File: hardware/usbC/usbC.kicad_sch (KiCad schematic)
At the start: 17 parts, among them J2 Conn_01x02, J3 Conn_01x02, J4 Conn_01x01, J5 Conn_01x02, J6 Conn_01x01, J7 Conn_01x01, J8 Conn_01x01, J9 Connector, USB-TYPE-C-16P, U1 USBLC6-2SC6, U2 AMS1117-3.3

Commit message: wip
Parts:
- removed J4, J6, J7, J8: Conn_01x01, Connector_PinHeader_1.00mm:PinHeader_1x01_P1.00mm_Vertical, symbol Connector_Generic:Conn_01x01
- added J1: Conn_01x02, LIB_S2B-ZR_LF__SN_:S2BZRLFSN, symbol Connector_Generic:Conn_01x02
- added J6, J7: Conn_01x02, Connector_PinHeader_2.54mm:PinHeader_1x02_P2.54mm_Vertical, symbol Connector_Generic:Conn_01x02
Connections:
- net D+: now also J6.1 (Pin_1)
- net D-: now also J6.2 (Pin_2)
- net GND: now also J1.2 (Pin_2), J7.1 (Pin_1)
- net VCC: now also J1.1 (Pin_1)
- net at F1.1, J9.A9B4 (VBUS), J9.B9A4 (VBUS): now also J7.2 (Pin_2)

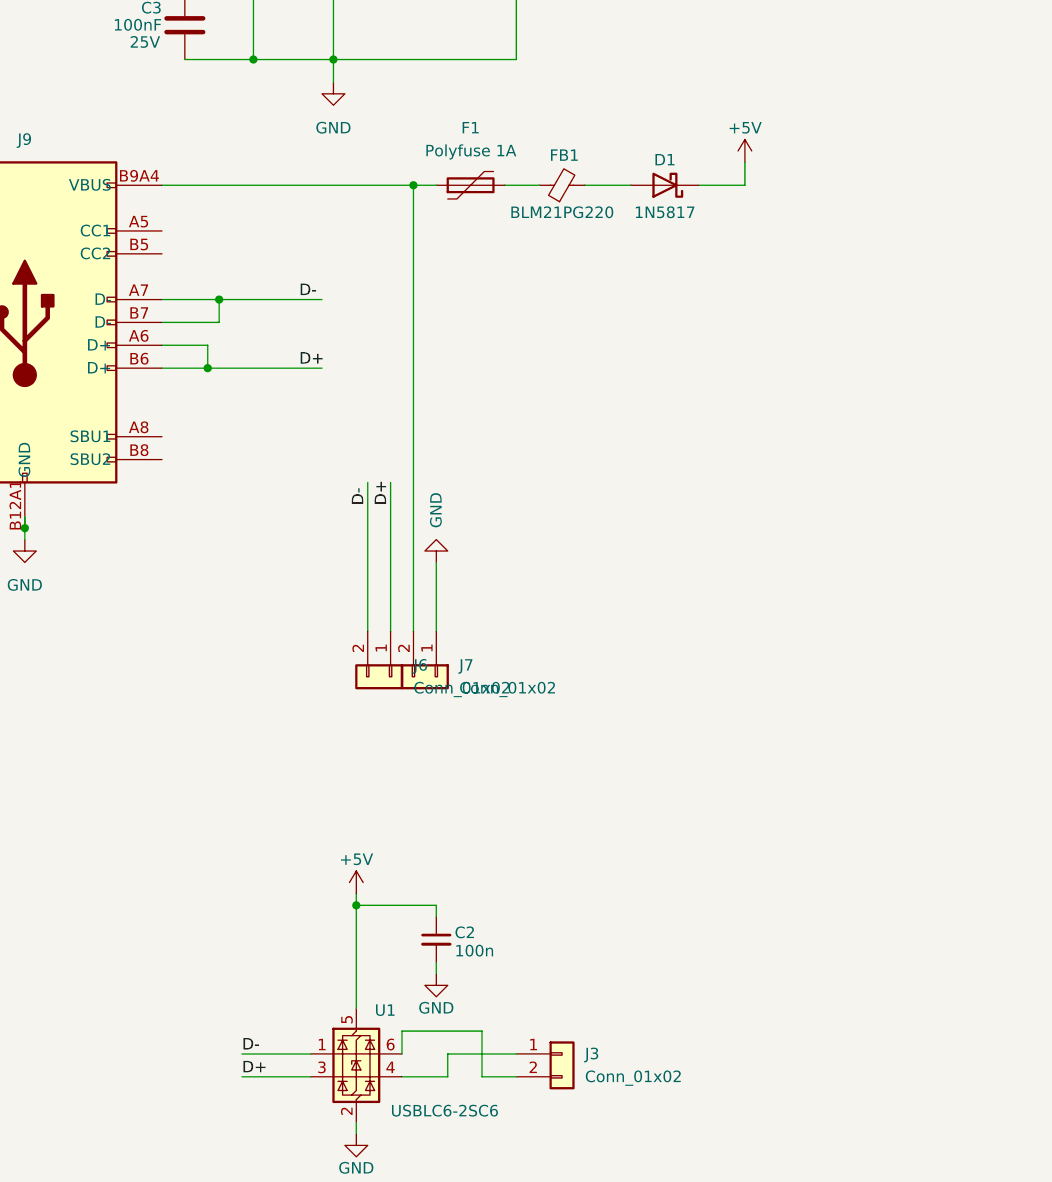
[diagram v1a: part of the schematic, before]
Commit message: usbc production
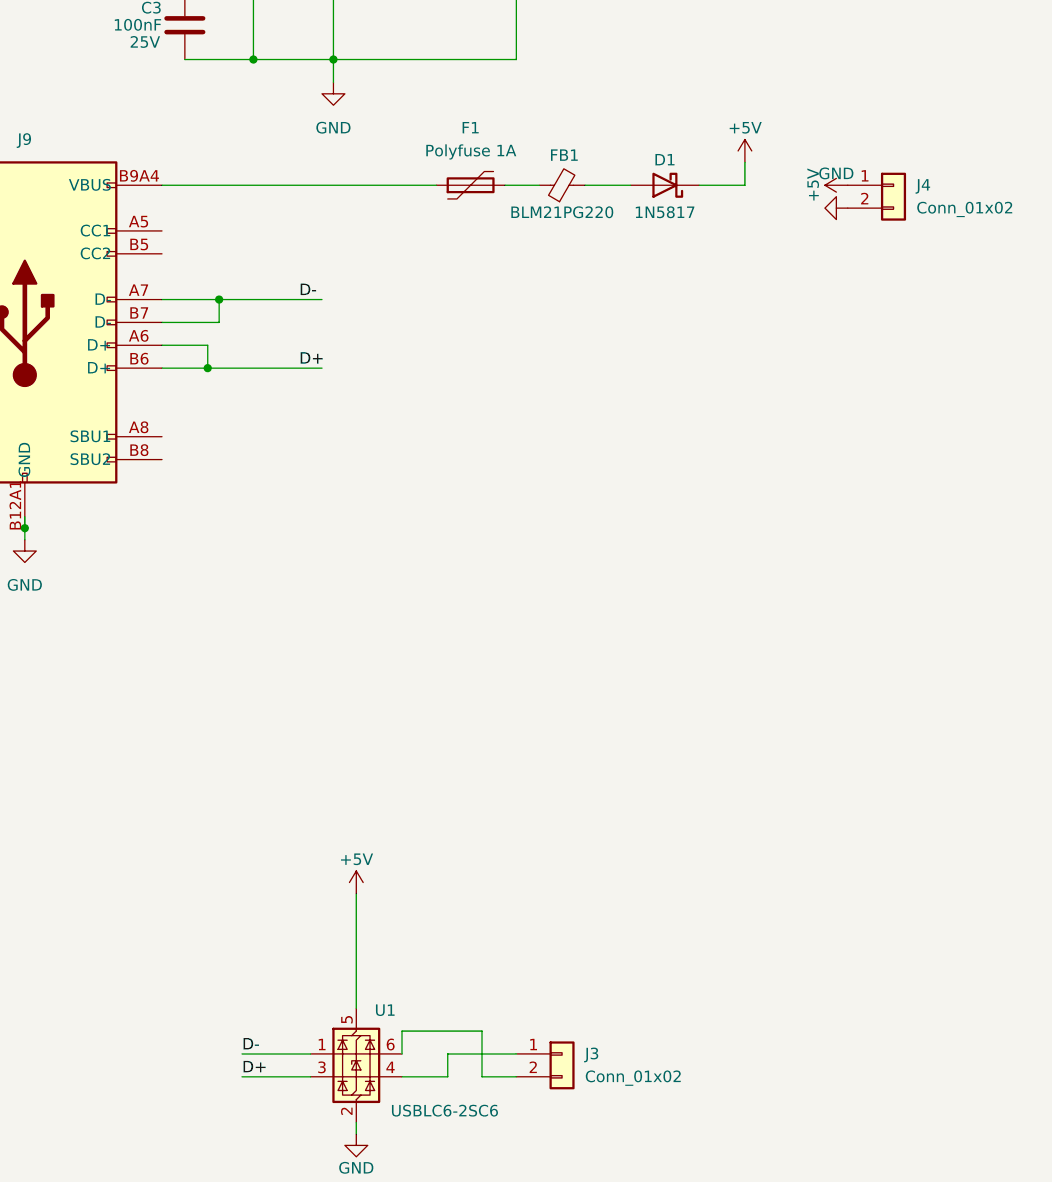
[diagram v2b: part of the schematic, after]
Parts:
- removed C2: 100n, Capacitor_SMD:C_0402_1005Metric_Pad0.74x0.62mm_HandSolder, symbol Morten_Library.kicad_sym_9:C_Small
- removed J6, J7: Conn_01x02, Connector_PinHeader_2.54mm:PinHeader_1x02_P2.54mm_Vertical, symbol Connector_Generic:Conn_01x02
- added J4: Conn_01x02, LIB_S2B-ZR_LF__SN_:S2BZRLFSN, symbol Connector_Generic:Conn_01x02
- C17, C18, C3: LCSC (none) -> C96446; LCSC Part # C96446 -> (none)
- F1: LCSC (none) -> C1020
- FB1: LCSC (none) -> C88993
- U1: LCSC (none) -> C2687116
- U2: LCSC (none) -> C7473143; LCSC Part # C7473143 -> (none)
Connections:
- net +5V: now also J4.1 (Pin_1)
- net GND: now also J4.2 (Pin_2)
